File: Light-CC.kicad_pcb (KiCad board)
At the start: 2 copper layers, 60 x 60 mm, 63 parts, among them J1 Conn_01x02_Pin, J2 Conn_01x02_Pin, J3 USB_C_Receptacle_USB2.0, J4 Conn_01x03_Male, Q1 BC547, Q2 BC547, Q3 BC547, Q4 BS870, Q5 STD7NK40Z, U1 LM1117-3.3, U3 W25Q64JVSSIQ, U4 RP2040, U5 LM1117-3.3, Y1 Crystal

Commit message: Done
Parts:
- added D3: SS14/SS34, Diode_SMD:D_SMA, B.Cu at (98.2, 93.3)
- added J5: Conn_01x02_Pin, Connector_Wire:SolderWire-0.1sqmm_1x02_P3.6mm_D0.4mm_OD1mm_Relief, F.Cu at (100.1, 90.4)
- added Q7: BS870, Package_TO_SOT_SMD:SOT-23, F.Cu at (104.2, 84.1)
- C13, R5: moved to B.Cu
- C5: moved to F.Cu
- moved C5 35.1 mm to (120.7, 102.0), turned to 90 degrees
- moved RST1 28.7 mm to (108.9, 103.8)
- moved C21 22.8 mm to (112.2, 78.5), turned to 90 degrees
- moved C22 20.6 mm to (114.9, 78.6), turned to 90 degrees
- moved C3 18.8 mm to (117.7, 78.6), turned to 90 degrees
- moved R5 13.3 mm to (131.2, 104.9), turned to -90 degrees
- moved C16 12.2 mm to (95.9, 101.4)
- moved R21 2.36 mm to (110.6, 89.5), turned to 0 degrees
- moved C20 2.06 mm to (112.7, 92.2), turned to 90 degrees
- moved C13 0.22 mm to (124.2, 106.9)
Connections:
- D1 pad 2: +5V -> +3V3
- U4 pad 29: unconnected-(U4-GPIO18-Pad29) -> /MCU/HAP_PWM
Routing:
- net GND: track 34.9 -> 340.7 mm, vias 0 -> 19
- net +3V3: track 104.2 -> 231.5 mm, vias 7 -> 13
- net Net-(U4-VREG_VOUT): track 6.20 -> 89.2 mm, vias 1 -> 7
- net /MCU/SS: track 6.51 -> 65.6 mm, vias 1 -> 3
- net /MCU/HAP_PWM: track 0.00 -> 40.3 mm, vias 0 -> 2
- net +5V: track 0.00 -> 23.3 mm, vias 0 -> 3
- net /MCU/LED1: track 22.6 -> 45.3 mm, vias 1 -> 2
- net /MCU/LED2: track 25.7 -> 44.2 mm, vias 1 -> 2
- net /MCU/LED3: track 27.4 -> 43.1 mm, vias 1 -> 4
- net +12V: track 85.9 -> 100.2 mm
- net Net-(D3-A): track 0.00 -> 14.0 mm
- net /MCU/MCU_BOOT: track 0.00 -> 10.4 mm, vias 0 -> 1
- net Net-(D2-A): track 33.5 -> 39.6 mm, vias 2 -> 3
- net unconnected-(U4-GPIO9-Pad12): track 0.00 -> 4.40 mm
- net unconnected-(U4-GPIO11-Pad14): track 0.00 -> 4.31 mm
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- added copper zone on B.Cu, net GND
- added copper zone on F.Cu, net GND
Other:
- board size 60 x 60 mm -> 60 x 48 mm

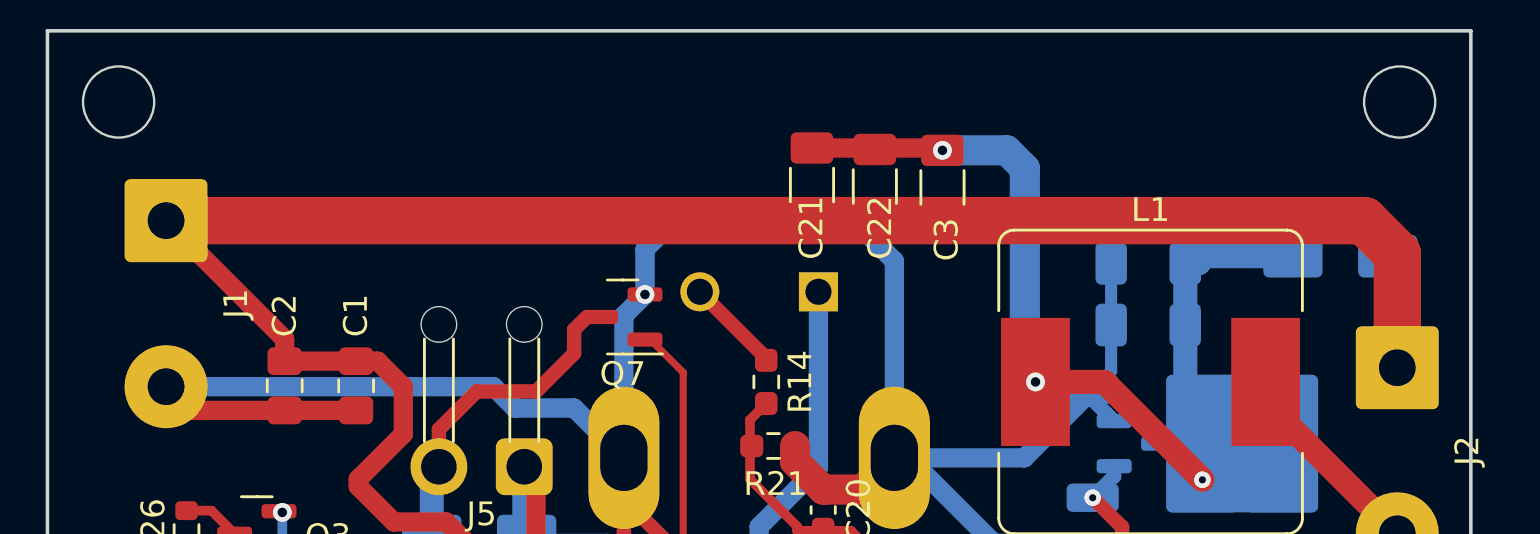
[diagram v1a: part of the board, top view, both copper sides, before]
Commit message: Added PolyFuse to output
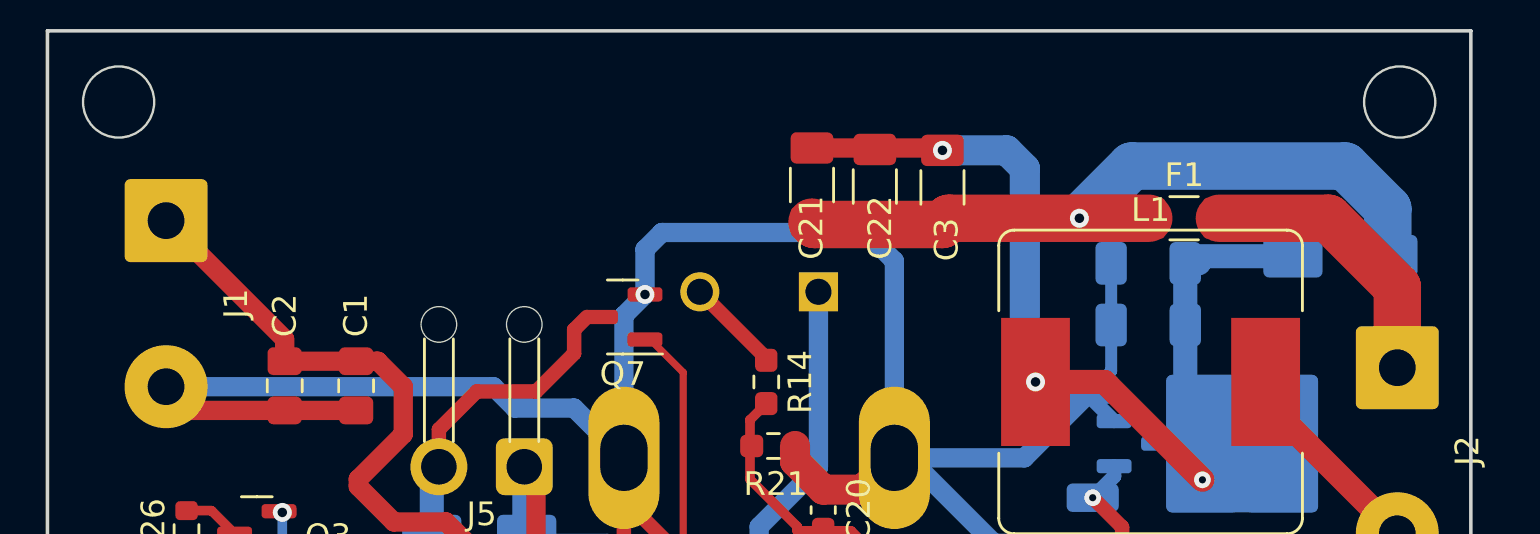
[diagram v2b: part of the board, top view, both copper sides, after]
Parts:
- added F1: Polyfuse, Fuse:Fuse_1206_3216Metric_Pad1.42x1.75mm_HandSolder, F.Cu at (127.9, 79.9)
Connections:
- J2 pad 1: +12V -> Net-(J2-Pin_1)
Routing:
- net +12V: track 100.2 -> 69.1 mm, vias 0 -> 1
- net Net-(J2-Pin_1): track 0.00 -> 12.7 mm
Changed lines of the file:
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@@
   (net 69 "unconnected-(U4-GPIO25-Pad37)")
   (net 70 "/MCU/HAP_PWM")
+  (net 71 "Net-(J2-Pin_1)")
   (footprint "Button_Switch_SMD:SW_SPST_SKQG_WithStem" (layer "F.Cu")
     (at 108.9 103.8)
@@
       (stroke (width 0.1) (type solid)) (fill none) (layer "F.Fab"))
     (pad "1" thru_hole roundrect (at 0 0 270) (size 3.5 3.5) (drill 1.55) (layers "*.Cu" "*.Mask") (roundrect_rratio 0.071429)
-      (net 58 "+12V") (pinfunction "Pin_1") (pintype "passive"))
+      (net 71 "Net-(J2-Pin_1)") (pinfunction "Pin_1") (pintype "passive"))
     (pad "2" thru_hole circle (at 7 0 270) (size 3.5 3.5) (drill 1.55) (layers "*.Cu" "*.Mask")
       (net 66 "Net-(J2-Pin_2)") (pinfunction "Pin_2") (pintype "passive"))
@@
     )
   )
+  (footprint "Fuse:Fuse_1206_3216Metric_Pad1.42x1.75mm_HandSolder" (layer "F.Cu")
+    (at 127.9125 79.9)
+    (descr "Fuse SMD 1206 (3216 Metric), square (rectangular) end terminal, IPC_7351 nominal with elongated pad for handsoldering. (Body size source: http://www.tortai-tech.com/upload/download/2011102023233369053.pdf), generated with kicad-footprint-generator")
+    (tags "fuse handsolder")
+    (property "Sheetfile" "Light-CC.kicad_sch")
+    (property "Sheetname" "")
+    (property "ki_description" "Resettable fuse, polymeric positive temperature coefficient")
+    (property "ki_keywords" "resettable fuse PTC PPTC polyfuse polyswitch")
+    (attr smd)
+    (fp_text reference "F1" (at 0 -1.82) (layer "F.SilkS")
+        (effects (font (size 1 1) (thickness 0.15)))
+    )
+    (fp_text value "Polyfuse" (at 0 1.82) (layer "F.Fab")
+        (effects (font (size 1 1) (thickness 0.15)))
+    )
+    (fp_text user "${REFERENCE}" (at 0 0) (layer "F.Fab")
+        (effects (font (size 0.8 0.8) (thickness 0.12)))
+    )
+    (fp_line (start -0.602064 -0.91) (end 0.602064 -0.91)
+      (stroke (width 0.12) (type solid)) (layer "F.SilkS"))
+    (fp_line (start -0.602064 0.91) (end 0.602064 0.91)
+      (stroke (width 0.12) (type solid)) (layer "F.SilkS"))
+    (fp_line (start -2.45 -1.12) (end 2.45 -1.12)
+      (stroke (width 0.05) (type solid)) (layer "F.CrtYd"))
+    (fp_line (start -2.45 1.12) (end -2.45 -1.12)
+      (stroke (width 0.05) (type solid)) (layer "F.CrtYd"))
+    (fp_line (start 2.45 -1.12) (end 2.45 1.12)
+      (stroke (width 0.05) (type solid)) (layer "F.CrtYd"))
+    (fp_line (start 2.45 1.12) (end -2.45 1.12)
+      (stroke (width 0.05) (type solid)) (layer "F.CrtYd"))
+    (fp_line (start -1.6 -0.8) (end 1.6 -0.8)
+      (stroke (width 0.1) (type solid)) (layer "F.Fab"))
+    (fp_line (start -1.6 0.8) (end -1.6 -0.8)
+      (stroke (width 0.1) (type solid)) (layer "F.Fab"))
+    (fp_line (start 1.6 -0.8) (end 1.6 0.8)
+      (stroke (width 0.1) (type solid)) (layer "F.Fab"))
+    (fp_line (start 1.6 0.8) (end -1.6 0.8)
+      (stroke (width 0.1) (type solid)) (layer "F.Fab"))
+    (pad "1" smd roundrect (at -1.4875 0) (size 1.425 1.75) (layers "F.Cu" "F.Paste" "F.Mask") (roundrect_rratio 0.175439)
+      (net 58 "+12V") (pintype "passive"))
+    (pad "2" smd roundrect (at 1.4875 0) (size 1.425 1.75) (layers "F.Cu" "F.Paste" "F.Mask") (roundrect_rratio 0.175439)
+      (net 71 "Net-(J2-Pin_1)") (pintype "passive"))
+    (model "${KICAD6_3DMODEL_DIR}/Fuse.3dshapes/Fuse_1206_3216Metric.wrl"
+      (offset (xyz 0 0 0))
+      (scale (xyz 1 1 1))
+      (rotate (xyz 0 0 0))
+    )
+  )
   (footprint "Capacitor_SMD:C_0603_1608Metric_Pad1.08x0.95mm_HandSolder" (layer "F.Cu")
     (at 102.6 100 180)
@@
   (segment (start 105.9125 97.5) (end 105.4125 98) (width 0.3048) (layer "F.Cu") (net 57))
   (segment (start 107.5 97.5) (end 105.9125 97.5) (width 0.3048) (layer "F.Cu") (net 57))
+  (segment (start 112.32675 80.1625) (end 112.22675 80.0625) (width 2) (layer "F.Cu") (net 58))
   (segment (start 98.65 103.9) (end 98.65 102.25) (width 0.8128) (layer "F.Cu") (net 58))
   (segment (start 95 87) (end 93.925 85.925) (width 0.8128) (layer "F.Cu") (net 58))
   (segment (start 98.65 102.25) (end 98.8 102.1) (width 0.8128) (layer "F.Cu") (net 58))
   (segment (start 90 85) (end 85 80) (width 0.8128) (layer "F.Cu") (net 58))
-  (segment (start 135.5 80) (end 136.9 81.4) (width 2) (layer "F.Cu") (net 58))
   (segment (start 93.1 90.9) (end 95 89) (width 0.8128) (layer "F.Cu") (net 58))
   (segment (start 90 85.925) (end 90 85) (width 0.8128) (layer "F.Cu") (net 58))
   (segment (start 93.1 91.2) (end 93.1 90.9) (width 0.8128) (layer "F.Cu") (net 58))
   (segment (start 98.65 103.9) (end 98.65 103.2) (width 0.6096) (layer "F.Cu") (net 58))
-  (segment (start 136.9 81.4) (end 136.9 86.2) (width 2) (layer "F.Cu") (net 58))
   (segment (start 98.8 94.7) (end 96.8 92.7) (width 0.8128) (layer "F.Cu") (net 58))
   (segment (start 94.6 92.7) (end 93.1 91.2) (width 0.8128) (layer "F.Cu") (net 58))
   (segment (start 96.8 92.7) (end 94.6 92.7) (width 0.8128) (layer "F.Cu") (net 58))
   (segment (start 95 89) (end 95 87) (width 0.8128) (layer "F.Cu") (net 58))
-  (segment (start 85 80) (end 135.5 80) (width 2) (layer "F.Cu") (net 58))
+  (segment (start 126.425 79.9) (end 117.98925 79.9) (width 2) (layer "F.Cu") (net 58))
   (segment (start 93.925 85.925) (end 93.01 85.925) (width 0.8128) (layer "F.Cu") (net 58))
   (segment (start 93.01 85.925) (end 90 85.925) (width 0.8128) (layer "F.Cu") (net 58))
+  (segment (start 117.72675 80.1625) (end 112.32675 80.1625) (width 2) (layer "F.Cu") (net 58))
   (segment (start 98.65 103.2) (end 96.85 101.4) (width 0.6096) (layer "F.Cu") (net 58))
   (segment (start 98.8 102.1) (end 98.8 94.7) (width 0.8128) (layer "F.Cu") (net 58))
-  (segment (start 136.5 81.5) (end 136.5 85.8) (width 1.016) (layer "B.Cu") (net 58))
-  (segment (start 136.5 85.8) (end 136.9 86.2) (width 1.016) (layer "B.Cu") (net 58))
+  (segment (start 117.98925 79.9) (end 117.72675 80.1625) (width 2) (layer "F.Cu") (net 58))
+  (via (at 123.5 79.9) (size 0.8) (drill 0.4) (layers "F.Cu" "B.Cu") (net 58))
+  (segment (start 123.5 79.9) (end 125.7 77.7) (width 2) (layer "B.Cu") (net 58))
+  (segment (start 136.5 79.5) (end 136.5 81.5) (width 2) (layer "B.Cu") (net 58))
+  (segment (start 125.7 77.7) (end 134.7 77.7) (width 2) (layer "B.Cu") (net 58))
+  (segment (start 134.7 77.7) (end 136.5 79.5) (width 2) (layer "B.Cu") (net 58))
   (segment (start 124.56 86.8) (end 128.685 90.925) (width 1.016) (layer "F.Cu") (net 59))
   (segment (start 121.65 86.8) (end 124.56 86.8) (width 1.016) (layer "F.Cu") (net 59))
@@
   (via (at 112.1 95) (size 0.8) (drill 0.4) (layers "F.Cu" "B.Cu") (net 70))
   (segment (start 126.7 95) (end 112.1 95) (width 0.3048) (layer "B.Cu") (net 70))
+  (segment (start 129.4 79.9) (end 134 79.9) (width 2) (layer "F.Cu") (net 71))
+  (segment (start 136.9 82.8) (end 136.9 86.2) (width 2) (layer "F.Cu") (net 71))
+  (segment (start 134 79.9) (end 136.9 82.8) (width 2) (layer "F.Cu") (net 71))
+  (segment (start 136.5 85.8) (end 136.9 86.2) (width 1.016) (layer "B.Cu") (net 71))
   (zone (net 1) (net_name "GND") (layers "F&B.Cu") (hatch edge 0.5)
     (connect_pads (clearance 0.5))

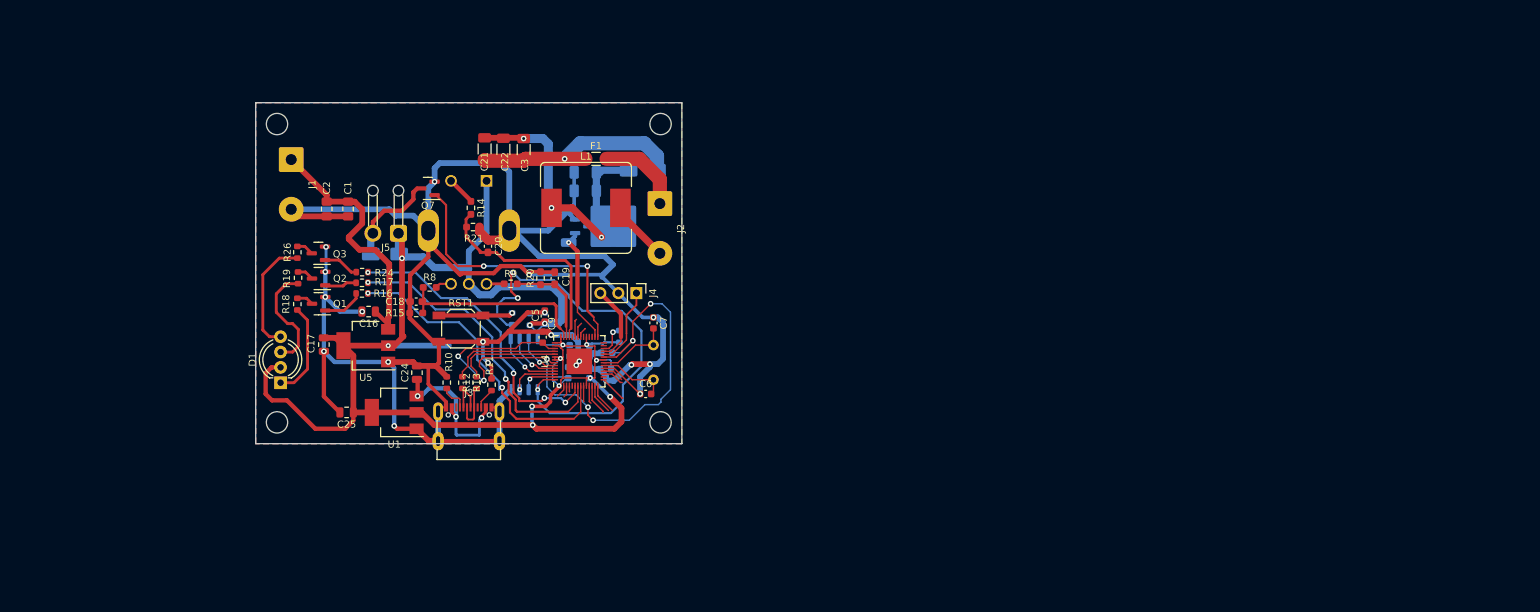
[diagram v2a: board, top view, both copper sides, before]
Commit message: Changed the layout based on Power supply
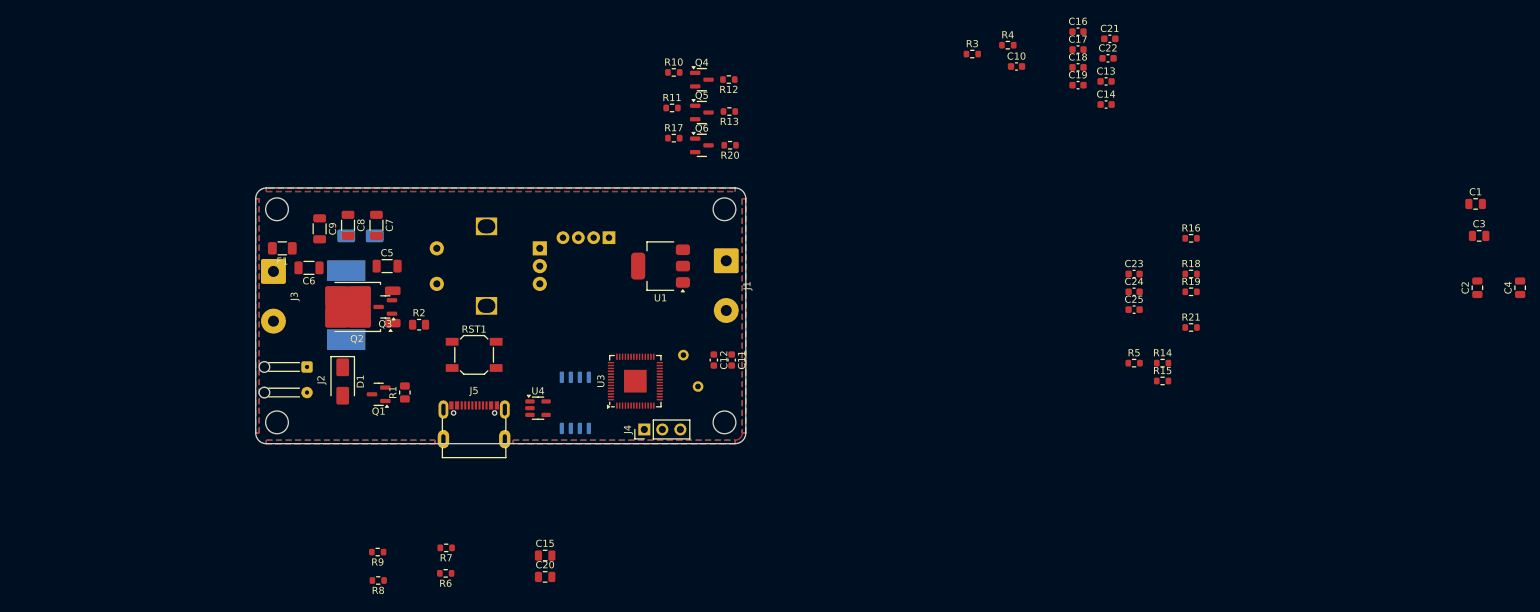
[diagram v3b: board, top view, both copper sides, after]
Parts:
- removed Q7: BS870, Package_TO_SOT_SMD:SOT-23
- removed R24: 4K7, Resistor_SMD:R_0603_1608Metric
- removed R26: 1K, Resistor_SMD:R_0603_1608Metric
- removed U5: LM1117-3.3, Package_TO_SOT_SMD:SOT-223-3_TabPin2
- added Q6: BC547, Package_TO_SOT_SMD:SOT-23, F.Cu at (142.8, 78.0)
- added R1: 100K, Resistor_SMD:R_0805_2012Metric, F.Cu at (101.0, 112.8)
- added R2: 100K, Resistor_SMD:R_0805_2012Metric, F.Cu at (103.0, 103.2)
- added R3: 1K, Resistor_SMD:R_0603_1608Metric, F.Cu at (180.9, 65.1)
- added R4: 10K, Resistor_SMD:R_0603_1608Metric, F.Cu at (185.9, 63.9)
- added U2: W25Q64JVSSIQ, Package_SO:SOIC-8_5.23x5.23mm_P1.27mm, B.Cu at (125.0, 114.2)
- C1: value C -> 10uf; footprint Capacitor_SMD:C_0805_2012Metric_Pad1.18x1.45mm_HandSolder -> Capacitor_SMD:C_0805_2012Metric
- C10, C13, C14, R5: moved to F.Cu
- C11, C12: value 100nf -> 20pf; moved to F.Cu
- C15: value 100nf -> 10uf; footprint Capacitor_SMD:C_0603_1608Metric -> Capacitor_SMD:C_0805_2012Metric; moved to F.Cu
- C16, C17: value 10uf -> 100nf; footprint Capacitor_SMD:C_0805_2012Metric -> Capacitor_SMD:C_0603_1608Metric
- C18, C19: value C -> 100nf; footprint Capacitor_SMD:C_0603_1608Metric_Pad1.08x0.95mm_HandSolder -> Capacitor_SMD:C_0603_1608Metric
- C2: footprint Capacitor_SMD:C_0805_2012Metric_Pad1.18x1.45mm_HandSolder -> Capacitor_SMD:C_0805_2012Metric
- C20: value C -> 10uf; footprint Capacitor_SMD:C_0603_1608Metric_Pad1.08x0.95mm_HandSolder -> Capacitor_SMD:C_0805_2012Metric
- C21, C22: value 100uf/50V -> 100nf; footprint Capacitor_SMD:C_1206_3216Metric_Pad1.33x1.80mm_HandSolder -> Capacitor_SMD:C_0603_1608Metric
- C23: value 100uf/50V -> C; footprint Capacitor_SMD:C_1206_3216Metric_Pad1.33x1.80mm_HandSolder -> Capacitor_SMD:C_0603_1608Metric; moved to F.Cu
- C24, C25: value 10uf -> C; footprint Capacitor_SMD:C_0805_2012Metric -> Capacitor_SMD:C_0603_1608Metric
- C3: value 100uf/50V -> 10uf; footprint Capacitor_SMD:C_1206_3216Metric_Pad1.33x1.80mm_HandSolder -> Capacitor_SMD:C_0805_2012Metric
- C4: value 220uf/50V -> C; footprint Capacitor_SMD:C_1206_3216Metric_Pad1.33x1.80mm_HandSolder -> Capacitor_SMD:C_0805_2012Metric; moved to F.Cu
- C5: value 100nf -> 220uf/50V; footprint Capacitor_SMD:C_0603_1608Metric -> Capacitor_SMD:C_1206_3216Metric
- C6, C7: value 20pf -> 100uf/50V; footprint Capacitor_SMD:C_0603_1608Metric -> Capacitor_SMD:C_1206_3216Metric
- C8: value 100nf -> 100uf/50V; footprint Capacitor_SMD:C_0603_1608Metric -> Capacitor_SMD:C_1206_3216Metric; moved to F.Cu
- C9: value 100nf -> 100uf/50V; footprint Capacitor_SMD:C_0603_1608Metric -> Capacitor_SMD:C_1206_3216Metric
- D1: value LED_RAGB -> SS14/SS34; footprint LED_THT:LED_D5.0mm-4_RGB_Wide_Pins -> Diode_SMD:D_SMA
- D3: value SS14/SS34 -> LED_RAGB; footprint Diode_SMD:D_SMA -> LED_THT:LED_D5.0mm-4_RGB_Wide_Pins
- F1: footprint Fuse:Fuse_1206_3216Metric_Pad1.42x1.75mm_HandSolder -> Fuse:Fuse_1206_3216Metric
- J2: footprint Connector_Wire:SolderWire-0.75sqmm_1x02_P7mm_D1.25mm_OD3.5mm -> Connector_Wire:SolderWire-0.1sqmm_1x02_P3.6mm_D0.4mm_OD1mm_Relief
- J3: value USB_C_Receptacle_USB2.0 -> Conn_01x02_Pin; footprint USB:USB_C_Receptacle_Palconn_UTC16-G -> Connector_Wire:SolderWire-0.75sqmm_1x02_P7mm_D1.25mm_OD3.5mm
- J5: value Conn_01x02_Pin -> USB_C_Receptacle_USB2.0; footprint Connector_Wire:SolderWire-0.1sqmm_1x02_P3.6mm_D0.4mm_OD1mm_Relief -> USB:USB_C_Receptacle_Palconn_UTC16-G
- L1: moved to B.Cu
- MT1: footprint Rotary:XDCR_PEC11R-4215F-S0024 -> Rotary_Encoder:RotaryEncoder_Alps_EC12E-Switch_Vertical_H20mm
- Q1, Q3: value BC547 -> BS870
- Q2: value BC547 -> STD7NK40Z; footprint Package_TO_SOT_SMD:SOT-23 -> Package_TO_SOT_SMD:TO-252-2
- Q4: value BS870 -> BC547; moved to F.Cu
- Q5: value STD7NK40Z -> BC547; footprint Package_TO_SOT_SMD:TO-252-2 -> Package_TO_SOT_SMD:SOT-23; moved to F.Cu
- R10, R11: value R_US -> 4K7
- R12, R13: value 27R -> 1K
- R14, R15, R21: footprint Resistor_SMD:R_0603_1608Metric_Pad0.98x0.95mm_HandSolder -> Resistor_SMD:R_0603_1608Metric
- R16: value 4K7 -> R_US
- R18, R19: value 1K -> R_US
- R20: value R_US -> 1K; footprint Resistor_SMD:R_0603_1608Metric_Pad0.98x0.95mm_HandSolder -> Resistor_SMD:R_0603_1608Metric
- R6: value 1K -> R_US; moved to F.Cu
- R7: value 10K -> R_US; moved to F.Cu
- R8, R9: value R_US -> 27R; footprint Resistor_SMD:R_0603_1608Metric_Pad0.98x0.95mm_HandSolder -> Resistor_SMD:R_0603_1608Metric
- U3: value W25Q64JVSSIQ -> RP2040; footprint Package_SO:SOIC-8_5.23x5.23mm_P1.27mm -> Package_DFN_QFN:QFN-56-1EP_7x7mm_P0.4mm_EP3.2x3.2mm; moved to F.Cu
- U4: value RP2040 -> MIC5219-3.3YM5; footprint RP2040:QFN-56-1EP_7x7mm_P0.4mm_EP5.6x5.6mm_copy -> Package_TO_SOT_SMD:SOT-23-5
- moved C2 162.4 mm to (252.0, 98.0), turned to 90 degrees
- moved C1 158.7 mm to (251.8, 86.2), turned to 0 degrees
- moved C3 135.1 mm to (252.2, 90.8), turned to 0 degrees
- moved C4 132.6 mm to (258.0, 98.0), turned to 90 degrees
- moved R18 125.9 mm to (211.7, 96.1), turned to 0 degrees
- moved R19 125.7 mm to (211.7, 98.6), turned to 0 degrees
- moved R16 117.0 mm to (211.7, 91.1), turned to 0 degrees
- moved C17 114.0 mm to (195.8, 64.5), turned to 0 degrees
- moved C25 111.8 mm to (203.7, 101.1), turned to 0 degrees
- moved C16 107.4 mm to (195.8, 62.0), turned to 0 degrees
- moved R15 105.5 mm to (207.7, 111.2), turned to 0 degrees
- moved R21 102.1 mm to (211.7, 103.6)
- moved C24 101.6 mm to (203.7, 98.6), turned to 0 degrees
- moved R14 99.8 mm to (207.7, 108.7), turned to 0 degrees
- moved C18 98.8 mm to (195.8, 67.0), turned to 0 degrees
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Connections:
- C11 pad 1: +3V3 -> GND
- C11 pad 2: GND -> Net-(U3-XIN)
- C12 pad 1: +3V3 -> GND
- C12 pad 2: GND -> Net-(U3-XOUT)
- C13 pad 1: +3V3 -> Net-(U3-VREG_VOUT)
- C14 pad 1: +3V3 -> Net-(U3-VREG_VOUT)
- C15 pad 1: +3V3 -> +5V
- C16 pad 1: +12V -> +3V3
- C18 pad 1: /MCU/RE1 -> +3V3
- C19 pad 1: /MCU/RE2 -> +3V3
- C20 pad 1: /MCU/RE_SW -> +3V3
- C21 pad 1: +12V -> +3V3
- C21 pad 2: Net-(D2-A) -> GND
- C22 pad 1: +12V -> +3V3
- C22 pad 2: Net-(D2-A) -> GND
- C23 pad 1: Net-(D2-A) -> /MCU/RE1
- C24 pad 1: +5V -> /MCU/RE2
- C25 pad 1: +3V3 -> /MCU/RE_SW
- C3 pad 1: +12V -> +3V3
- C3 pad 2: Net-(D2-A) -> GND
- C4 pad 1: Net-(D2-A) -> +12V
- C5 pad 1: +3V3 -> Net-(D2-A)
- C6 pad 1: GND -> Net-(D2-A)
- C6 pad 2: Net-(U4-XIN) -> GND
- C7 pad 1: GND -> +12V
- C7 pad 2: Net-(U4-XOUT) -> Net-(D2-A)
- C8 pad 1: Net-(U4-VREG_VOUT) -> +12V
- C8 pad 2: GND -> Net-(D2-A)
- C9 pad 1: Net-(U4-VREG_VOUT) -> +12V
- C9 pad 2: GND -> Net-(D2-A)
- D1 pad 1: /MCU/R1 -> +3V3
- D1 pad 2: +3V3 -> Net-(D1-A)
- D3 pad 1: +3V3 -> /MCU/R1
- D3 pad 2: Net-(D3-A) -> +3V3
- F1 pad 2: Net-(J2-Pin_1) -> Net-(J3-Pin_1)
- J2 pad 1: Net-(J2-Pin_1) -> +3V3
- J2 pad 2: Net-(J2-Pin_2) -> Net-(D1-A)
- L1 pad 2: Net-(J2-Pin_2) -> Net-(J3-Pin_2)
- Q1 pad 1: Net-(Q1-B) -> /MCU/HAP_PWM
- Q1 pad 3: Net-(Q1-C) -> Net-(D1-A)
- Q2 pad 1: Net-(Q2-B) -> /MCU/LED_PWM
- Q2 pad 2: GND -> Net-(D2-A)
- Q2 pad 3: Net-(Q2-C) -> GND
- Q3 pad 1: Net-(Q3-B) -> /MCU/LED_PWM
- Q3 pad 3: Net-(Q3-C) -> Net-(D2-A)
- Q4 pad 1: /MCU/LED_PWM -> Net-(Q4-B)
- Q4 pad 3: Net-(D2-A) -> Net-(Q4-C)
- Q5 pad 1: /MCU/LED_PWM -> Net-(Q5-B)
- Q5 pad 2: Net-(D2-A) -> GND
- Q5 pad 3: GND -> Net-(Q5-C)
- R10 pad 1: Net-(J3-CC1) -> /MCU/LED1
- R10 pad 2: GND -> Net-(Q4-B)
- R11 pad 1: Net-(J3-CC2) -> /MCU/LED2
- R11 pad 2: GND -> Net-(Q5-B)
- R12 pad 1: /MCU/D+ -> /MCU/R1
- R12 pad 2: /MCU/M_D+ -> Net-(Q4-C)
- R13 pad 1: /MCU/D- -> /MCU/G1
- R13 pad 2: /MCU/M_D- -> Net-(Q5-C)
- R14 pad 1: Net-(MT1-Pad2) -> /MCU/RE1
- R14 pad 2: /MCU/RE_SW -> Net-(MT1-PadB)
- R16 pad 1: /MCU/LED1 -> Net-(MT1-PadA)
- R16 pad 2: Net-(Q1-B) -> /MCU/RE2
- R17 pad 1: /MCU/LED2 -> /MCU/LED3
- R17 pad 2: Net-(Q2-B) -> Net-(Q6-B)
- R18 pad 1: /MCU/R1 -> Net-(MT1-Pad2)
- R18 pad 2: Net-(Q1-C) -> /MCU/RE_SW
- R19 pad 1: /MCU/G1 -> /MCU/RE2
- R19 pad 2: Net-(Q2-C) -> GND
- R20 pad 1: /MCU/RE2 -> /MCU/B1
- R20 pad 2: GND -> Net-(Q6-C)
- R6 pad 1: /MCU/SS -> Net-(J5-CC1)
- R6 pad 2: /MCU/MCU_BOOT -> GND
- R7 pad 1: /MCU/SS -> Net-(J5-CC2)
- R7 pad 2: +3V3 -> GND
- R8 pad 1: /MCU/RE1 -> /MCU/D+
- R8 pad 2: Net-(MT1-PadB) -> /MCU/M_D+
- R9 pad 1: Net-(MT1-PadA) -> /MCU/D-
- R9 pad 2: /MCU/RE2 -> /MCU/M_D-
- U1 pad 3: +5V -> +12V
- U3 pad 1: /MCU/SS -> +3V3
- U3 pad 2: /MCU/SD1 -> unconnected-(U3-GPIO0-Pad2)
- U3 pad 3: /MCU/SD2 -> unconnected-(U3-GPIO1-Pad3)
- U3 pad 4: GND -> unconnected-(U3-GPIO2-Pad4)
- U3 pad 5: /MCU/SD0 -> unconnected-(U3-GPIO3-Pad5)
- U3 pad 6: /MCU/SCLK -> /MCU/LED3
- U3 pad 7: /MCU/SD3 -> /MCU/LED2
- U3 pad 8: +3V3 -> /MCU/LED1
- U4 pad 1: +3V3 -> +5V
- U4 pad 2: unconnected-(U4-GPIO0-Pad2) -> GND
- U4 pad 3: unconnected-(U4-GPIO1-Pad3) -> +5V
- U4 pad 5: unconnected-(U4-GPIO3-Pad5) -> +3V3
- Y1 pad 1: Net-(U4-XOUT) -> Net-(U3-XOUT)
- Y1 pad 2: Net-(U4-XIN) -> Net-(U3-XIN)
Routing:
- net GND: track 340.7 -> 0.00 mm, vias 19 -> 0
- net +3V3: track 231.5 -> 0.00 mm, vias 13 -> 0
- net Net-(U4-VREG_VOUT): track 89.2 -> 0.00 mm, vias 7 -> 0
- net +12V: track 69.1 -> 0.00 mm, vias 1 -> 0
- net /MCU/SS: track 65.6 -> 0.00 mm, vias 3 -> 0
- net /MCU/LED1: track 45.3 -> 0.00 mm, vias 2 -> 0
- net /MCU/LED2: track 44.2 -> 0.00 mm, vias 2 -> 0
- net /MCU/LED3: track 43.1 -> 0.00 mm, vias 4 -> 0
- net /MCU/HAP_PWM: track 40.3 -> 0.00 mm, vias 2 -> 0
- net Net-(D2-A): track 39.6 -> 0.00 mm, vias 3 -> 0
- net /MCU/RE_SW: track 30.1 -> 0.00 mm
- net /MCU/RE1: track 27.5 -> 0.00 mm
- net +5V: track 23.3 -> 0.00 mm, vias 3 -> 0
- net /MCU/LED_PWM: track 16.5 -> 0.00 mm, vias 1 -> 0
- net /MCU/B1: track 16.5 -> 0.00 mm
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- added copper zone on B.Cu, net (none)
- added copper zone on F.Cu, net (none)
- removed copper zone on B.Cu, net GND
- removed copper zone on F.Cu, net GND
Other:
- board size 60 x 48 mm -> 69 x 36 mm
